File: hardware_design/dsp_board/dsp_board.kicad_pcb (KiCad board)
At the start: 2 copper layers, 57 x 53 mm, 72 parts, among them J1 USB4800-03-A_REVA, J2 SM06B-SRSS-TB(LF)(SN), J3 RCJ-041, J4 RCJ-041, J5 RCJ-041, J6 RCJ-041, J7 RCJ-041, J8 RCJ-041, Q1 BC807, U1 TPD2S017DBVR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

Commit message: Fixed logo
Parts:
- removed the REF** at (58.0, 111.0)
- added REF**: EasyDSP logo, easydsp_footprints:EasyDSP logo, F.Cu at (58.0, 113.0)

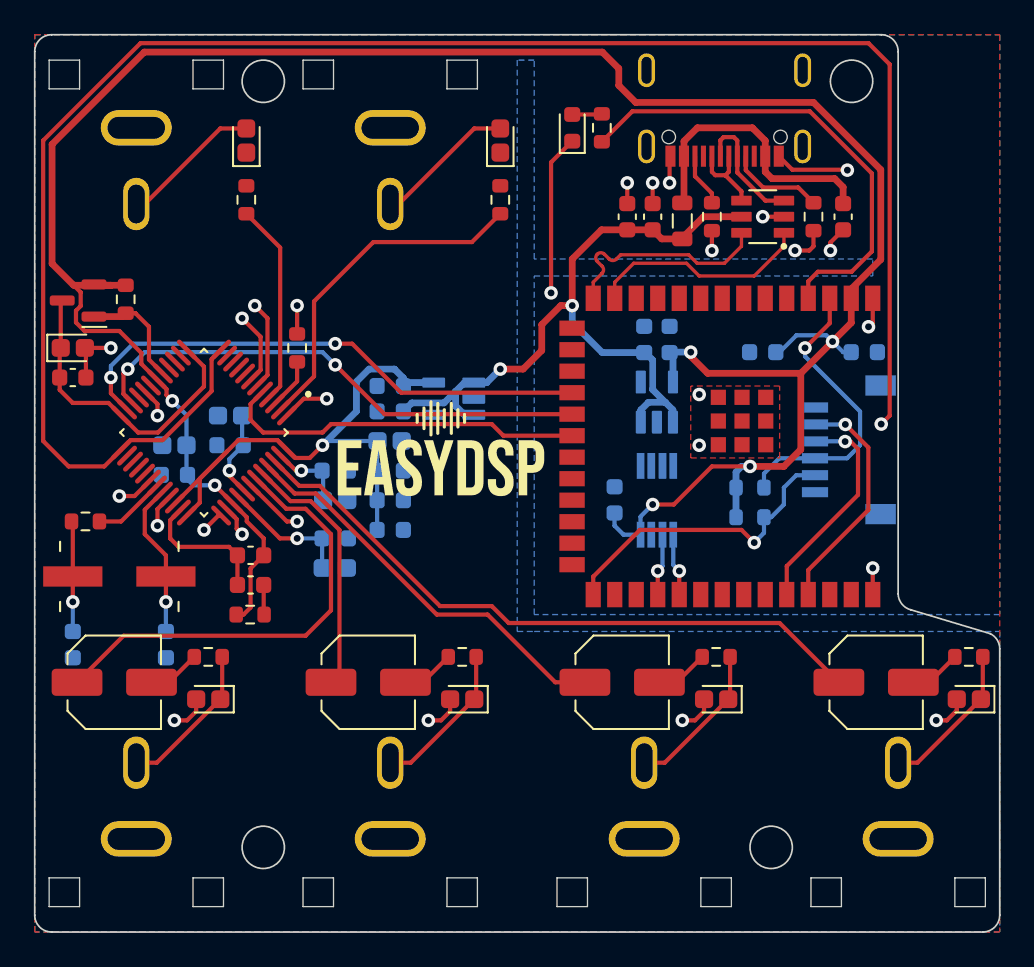
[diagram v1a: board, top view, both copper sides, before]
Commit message: Changed RCA connectors
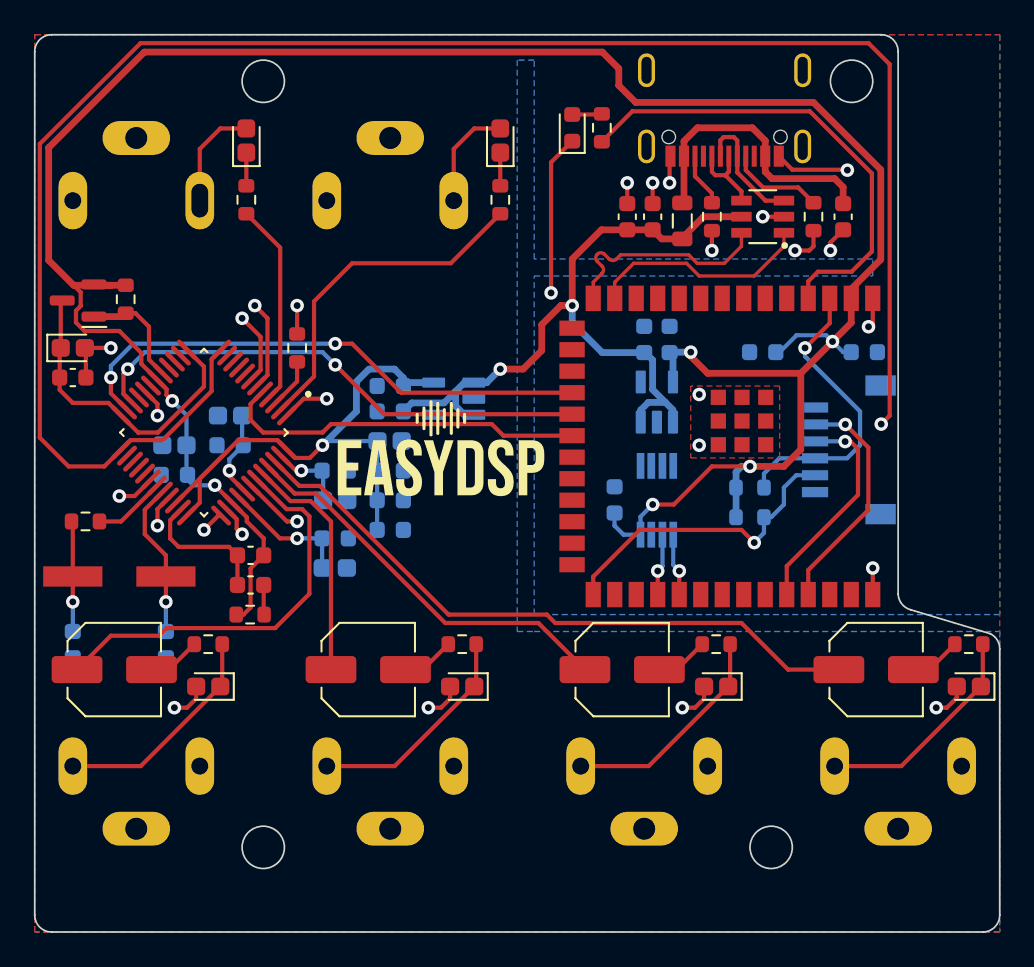
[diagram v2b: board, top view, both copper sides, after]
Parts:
- J3, J4, J5, J6, J7, J8: value RCJ-041 -> PJRAN1X1U01AUX; footprint RCJ-041:CUI_RCJ-041 -> PJRAN1X1U01AUX:PJRAN1X1U01X
- moved J3 7.00 mm to (55.0, 97.0), turned to -90 degrees
- moved J4 7.00 mm to (85.0, 133.0), turned to 90 degrees
- moved J5 7.00 mm to (55.0, 133.0), turned to 90 degrees
- moved J6 7.00 mm to (40.0, 97.0), turned to -90 degrees
- moved J7 7.00 mm to (70.0, 133.0), turned to 90 degrees
- moved J8 7.00 mm to (40.0, 133.0), turned to 90 degrees
- moved C30 0.75 mm to (83.7, 126.0)
- moved C31 0.75 mm to (53.7, 126.0)
- moved C32 0.75 mm to (89.2, 127.0)
- moved C33 0.75 mm to (59.2, 127.0)
- moved C35 0.75 mm to (68.7, 126.0)
- moved C36 0.75 mm to (38.7, 126.0)
- moved C37 0.75 mm to (74.2, 127.0)
- moved C38 0.75 mm to (44.2, 127.0)
- moved R10 0.75 mm to (89.2, 124.5)
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- renumbered R15 to R14, R14 to R15
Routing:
- net Net-(C38-Pad1): track 9.06 -> 13.2 mm
- net Net-(C33-Pad1): track 9.06 -> 13.2 mm
- net Net-(C37-Pad1): track 9.06 -> 13.2 mm
- net Net-(C32-Pad1): track 8.99 -> 13.1 mm
- net vout3: track 27.0 -> 24.1 mm
- net Net-(C34-Pad2): track 8.35 -> 6.30 mm
- net Net-(C29-Pad2): track 8.35 -> 6.30 mm
- net Net-(C34-Pad1): track 0.00 -> 1.96 mm
- net Net-(C29-Pad1): track 0.00 -> 1.96 mm
